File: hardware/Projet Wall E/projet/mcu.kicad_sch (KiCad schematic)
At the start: 11 parts, among them J3 Conn_01x06_Pin, U4 STM32G431RBTx

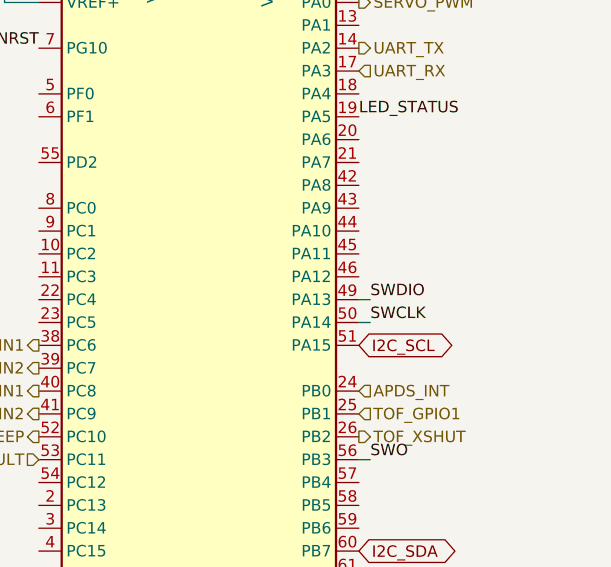
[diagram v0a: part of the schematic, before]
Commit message: Alim : BQ25896 + BQ27220, symboles perso wall_e, USB vers MCU
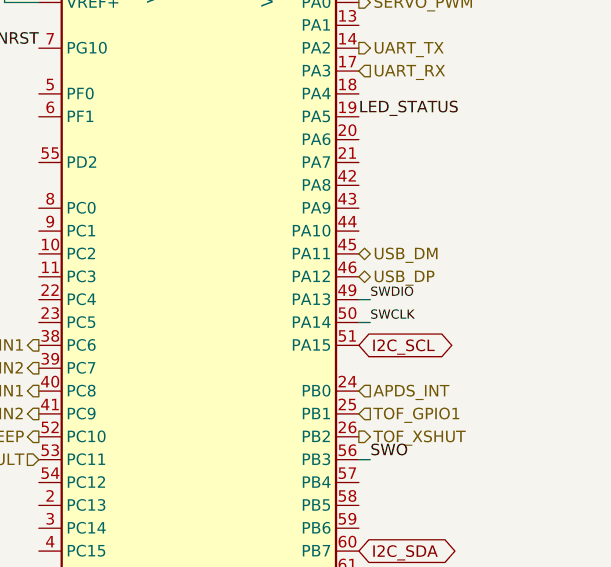
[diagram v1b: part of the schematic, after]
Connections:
- net USB_DM: now reaches U4.45 (PA11)
- net USB_DP: now reaches U4.46 (PA12)
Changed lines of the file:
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@@
 		(effects
 			(font
-				(size 1.27 1.27)
+				(size 1.016 1.016)
 			)
 			(justify left bottom)
@@
 		(effects
 			(font
-				(size 1.27 1.27)
+				(size 1.016 1.016)
 			)
 			(justify left bottom)
@@
 		)
 	)
+	(hierarchical_label "USB_DM"
+		(shape bidirectional)
+		(at 171.45 91.44 0)
+		(effects
+			(font
+				(size 1.27 1.27)
+			)
+			(justify left)
+		)
+	)
 	(hierarchical_label "MOT_AIN1"
 		(shape output)
@@
 		(effects
 			(font
+				(size 1.27 1.27)
+			)
+			(justify left)
+		)
+	)
+	(hierarchical_label "USB_DP"
+		(shape bidirectional)
+		(at 171.45 93.98 0)
+		(effects
+			(font

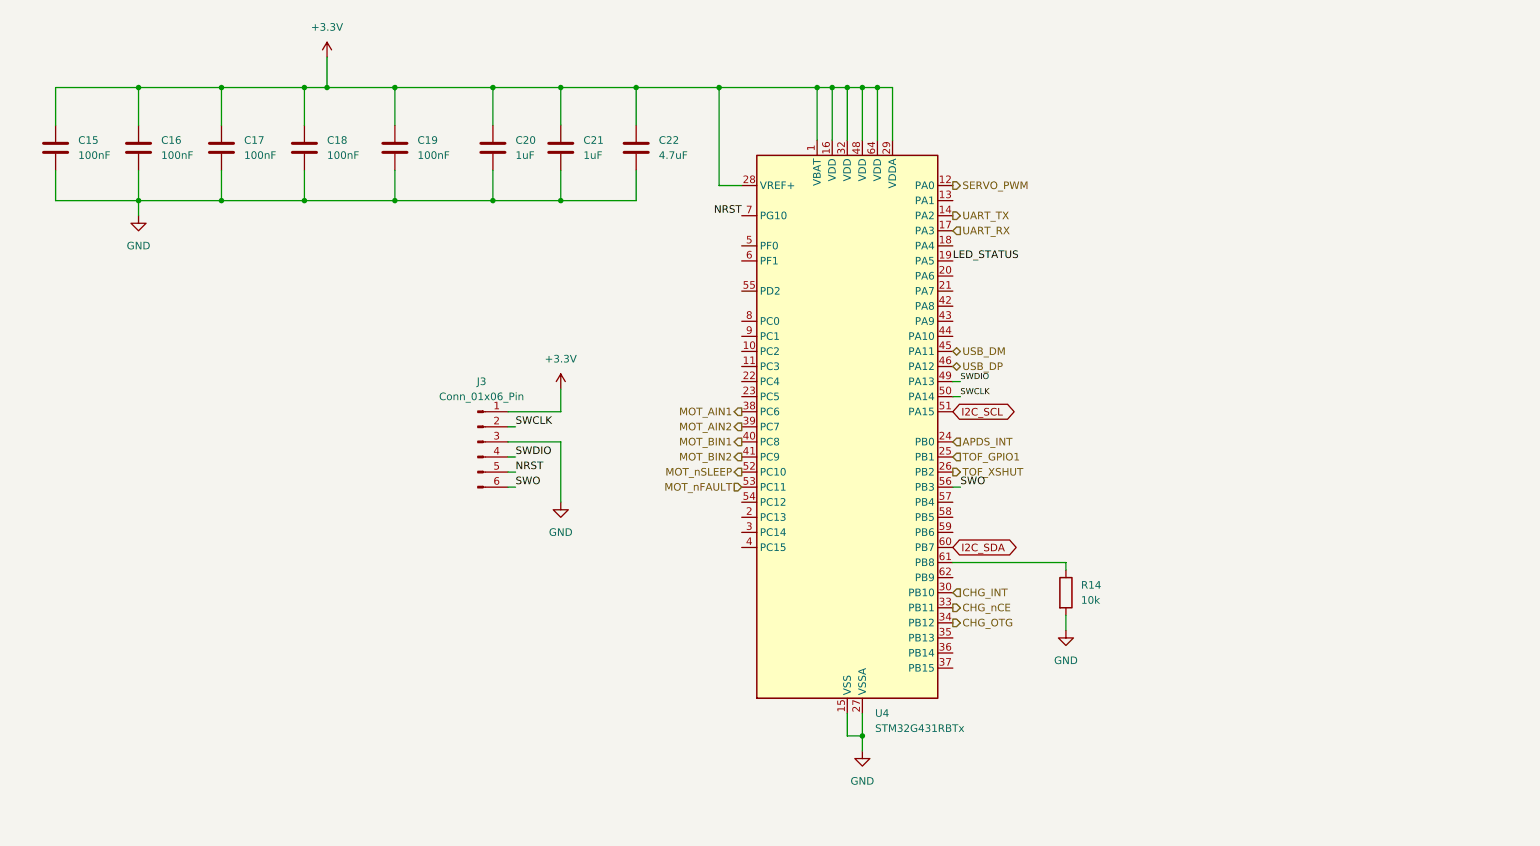
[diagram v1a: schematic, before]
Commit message: Mise à jour MCU + ajout du fichier .ioc
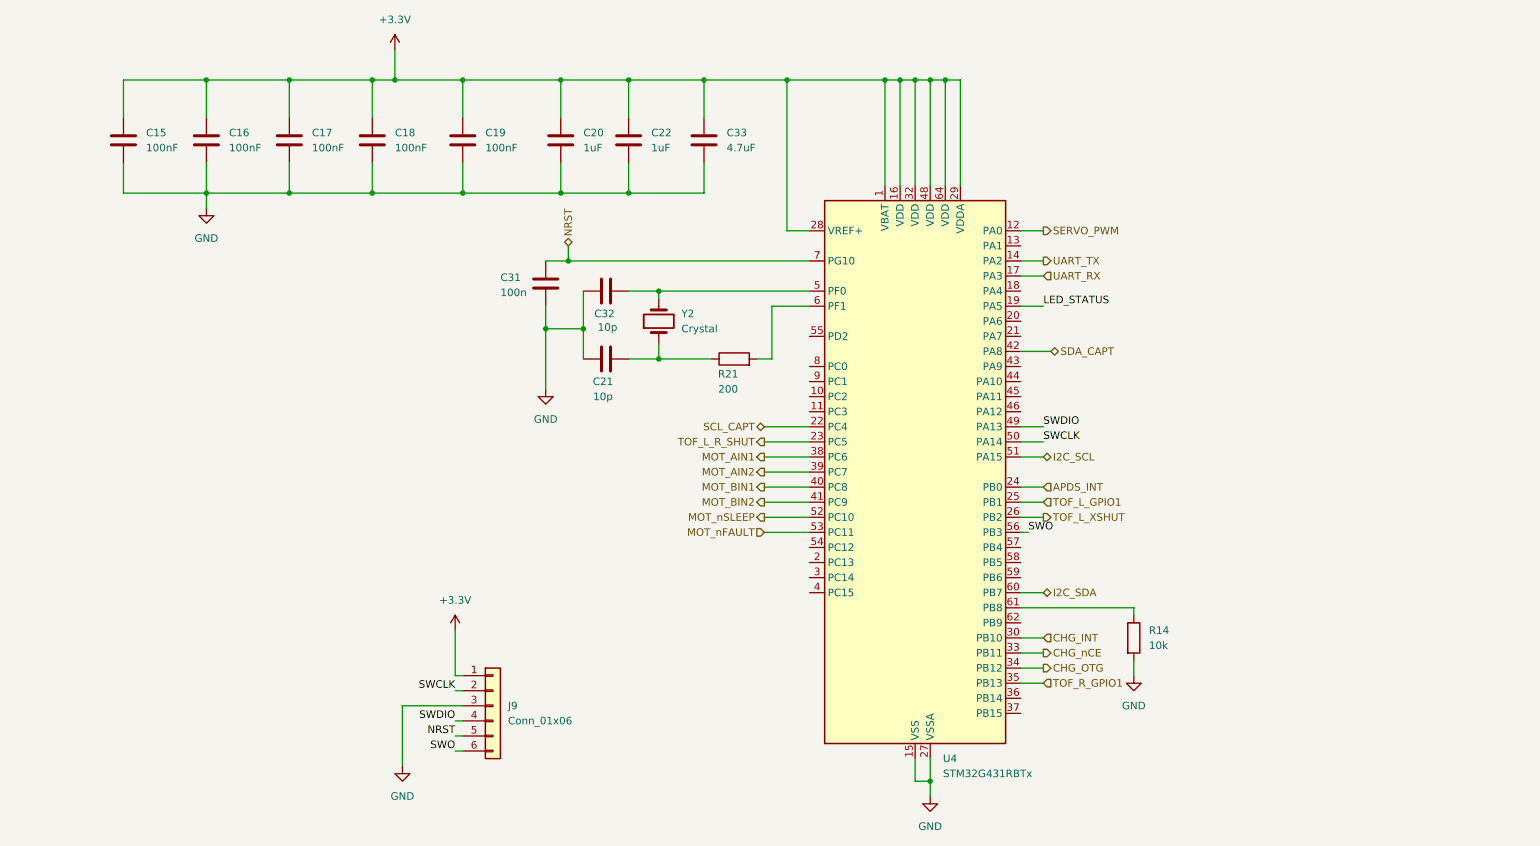
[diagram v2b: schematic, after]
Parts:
- removed J3: Conn_01x06_Pin, Connector_PinHeader_2.54mm:PinHeader_1x06_P2.54mm_Vertical, symbol wall_e:Conn_01x06_Pin
- added C31: 100n, Capacitor_SMD:C_0603_1608Metric, symbol wall_e:C
- added C32: 10p, Capacitor_SMD:C_0402_1005Metric, symbol wall_e:C
- added C33: 4.7uF, Capacitor_SMD:C_0603_1608Metric, symbol wall_e:C
- added J9: Conn_01x06, Connector_JST:JST_EH_S6B-EH_1x06_P2.50mm_Horizontal, symbol Connector_Generic:Conn_01x06
- added R21: 200, Resistor_SMD:R_0402_1005Metric, symbol wall_e:R
- added Y2: Crystal, symbol Device:Crystal
- C21: value 1uF -> 10p
- C22: value 4.7uF -> 1uF; footprint Capacitor_SMD:C_0603_1608Metric -> Capacitor_SMD:C_0402_1005Metric
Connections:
- net +3.3V: now also C33.1, J9.1 (Pin_1); no longer C21.1
- net GND: now also C21.1, C31.2, C32.1, C33.2, J9.3 (Pin_3); no longer C21.2
- net NRST: now also C31.1, J9.5 (Pin_5)
- net SWCLK: now also J9.2 (Pin_2)
- net SWDIO: now also J9.4 (Pin_4)
- net SWO: now also J9.6 (Pin_6)
- net SCL_CAPT: now reaches U4.22 (PC4)
- net TOF_L_R_SHUT: now reaches U4.23 (PC5)
- net TOF_R_GPIO1: now reaches U4.35 (PB13)
- net SDA_CAPT: now reaches U4.42 (PA8)
- net at U4.5 (PF0): now also C32.2, Y2.2
- net at U4.6 (PF1): now also R21.2
- net TOF_GPIO1 renamed TOF_L_GPIO1
- net TOF_XSHUT renamed TOF_L_XSHUT
- net USB_DM: no longer names the net of U4.45 (PA11)
- net USB_DP: no longer names the net of U4.46 (PA12)
- new net: C21.2, R21.1, Y2.1

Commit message: Add files via upload
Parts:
- removed J9: Conn_01x06, Connector_JST:JST_EH_S6B-EH_1x06_P2.50mm_Horizontal, symbol Connector_Generic:Conn_01x06
- removed R14: 10k, Resistor_SMD:R_01005_0402Metric, symbol wall_e:R
- removed R21: 200, Resistor_SMD:R_0402_1005Metric, symbol wall_e:R
- removed Y2: Crystal, symbol Device:Crystal
- added C23: 1uF, Capacitor_SMD:C_0402_1005Metric, symbol wall_e:C
- added D1: STATUS, LED_SMD:LED_0603_1608Metric, symbol Device:LED_Small
- added D2: POWER, LED_SMD:LED_0603_1608Metric, symbol Device:LED_Small
- added J1: Conn_01x03, Connector_Audio:Jack_XLR_Neutrik_NC3FAAH_Horizontal, symbol Connector_Generic:Conn_01x03
- added J2: Conn_ST_STDC14, Connector_PinHeader_1.27mm:PinHeader_2x07_P1.27mm_Vertical_SMD, symbol Connector:Conn_ST_STDC14
- added JP1, JP2: SolderJumper_2_Open, Jumper:SolderJumper-2_P1.3mm_Open_TrianglePad1.0x1.5mm, symbol Jumper:SolderJumper_2_Open
- added R3, R4: 1k, Resistor_SMD:R_0402_1005Metric, symbol Device:R_Small
- added Y1: 16MHz, Crystal:Crystal_SMD_EuroQuartz_MT-4Pin_3.2x2.5mm, symbol Device:Crystal_GND24_Small
- C19: value 100nF -> 4.7u
- C20: value 1uF -> 10n
- C33: value 4.7uF -> 100n
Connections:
- net +3.3V: now also C23.1, J1.1 (Pin_1), J2.3 (VCC), R3.1
- net GND: now also C23.2, D1.1 (K), D2.1 (K), J1.3 (Pin_3), J2.11 (GNDDetect), J2.5 (GND), J2.7 (GND), Y1.2 (G), Y1.4 (G)
- net LED_STATUS: now also R4.1
- net NRST: now also J2.12 (~{RST})
- net SERVO_PWM: now also U4.59 (PB6), J1.2 (Pin_2); no longer U4.12 (PA0)
- net SWCLK: now also J2.6 (JCLK/SWCLK)
- net SWDIO: now also J2.4 (JTMS/SWDIO)
- net SWO: now also J2.8 (JTDO/SWO)
- net ENCB_AOUT: now reaches U4.61 (PB8)
- net at C21.2: now also U4.6 (PF1), Y1.3
- net at C32.2, U4.5 (PF0): now also Y1.1
- net ENCB_BOUT: now reaches U4.43 (PA9)
- net ENCA_BOUT: now reaches U4.44 (PA10)
- net ENCA_AOUT: now reaches U4.62 (PB9)
- net TOF_L_R_SHUT renamed TOF_R_SHUT
- net UART_RX renamed VCP_RX
- net VCP_RX: now also JP1.1 (A)
- net UART_TX renamed VCP_TX
- net VCP_TX: now also JP2.1 (A)
- new net: J2.13 (VCP_RX), JP1.2 (B)
- new net: D1.2 (A), R4.2
- new net: J2.14 (VCP_TX), JP2.2 (B)
- new net: D2.2 (A), R3.2
- no-connect marks 0 -> 2
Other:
- moved on the sheet: C15, C16, C17, C18, C19, C20, C21, C22, C32, C33

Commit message: feat: mise a jour alim reference jlcpcb
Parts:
- C15, C16, C17, C18: JLCPCB Part # (none) -> C1525
- C20: JLCPCB Part # (none) -> C15195
- U4: JLCPCB Part # (none) -> C431633
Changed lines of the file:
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@@
 		)
 		(instances
+			(project "projet"
+				(path "/aad9219d-d686-4d68-8dbb-b3c2b0727159/8d7235a3-ed0d-4c0c-a716-b22c65fe70a8"
+					(reference "J1")
+					(unit 1)
+				)
+			)
 			(project "mcu"
 				(path "/d1f6b90d-1ee5-4a93-8c97-f2b0d96541e8"
@@
 		)
 		(instances
+			(project "projet"
+				(path "/aad9219d-d686-4d68-8dbb-b3c2b0727159/8d7235a3-ed0d-4c0c-a716-b22c65fe70a8"
+					(reference "#PWR016")
+					(unit 1)
+				)
+			)
 			(project "mcu"
 				(path "/d1f6b90d-1ee5-4a93-8c97-f2b0d96541e8"
@@
 			)
 		)
+		(property "JLCPCB Part #" "C15195"
+			(at 88.9 55.88 0)
+			(hide yes)
+			(show_name no)
+			(do_not_autoplace no)
+			(effects
+				(font
+					(size 1.27 1.27)
+				)
+			)
+		)
 		(pin "2"
 		)
@@
 		)
 		(instances
+			(project "projet"
+				(path "/aad9219d-d686-4d68-8dbb-b3c2b0727159/8d7235a3-ed0d-4c0c-a716-b22c65fe70a8"
+					(reference "JP1")
+					(unit 1)
+				)
+			)
 			(project "mcu"
 				(path "/d1f6b90d-1ee5-4a93-8c97-f2b0d96541e8"
@@
 		)
 		(instances
+			(project "projet"
+				(path "/aad9219d-d686-4d68-8dbb-b3c2b0727159/8d7235a3-ed0d-4c0c-a716-b22c65fe70a8"
+					(reference "#PWR034")
+					(unit 1)
+				)
+			)
 			(project "mcu"
 				(path "/d1f6b90d-1ee5-4a93-8c97-f2b0d96541e8"
@@
 		)
 		(instances
+			(project "projet"
+				(path "/aad9219d-d686-4d68-8dbb-b3c2b0727159/8d7235a3-ed0d-4c0c-a716-b22c65fe70a8"
+					(reference "#PWR017")
+					(unit 1)
+				)
+			)
 			(project "mcu"
 				(path "/d1f6b90d-1ee5-4a93-8c97-f2b0d96541e8"
@@
 		)
 		(instances
+			(project "projet"
+				(path "/aad9219d-d686-4d68-8dbb-b3c2b0727159/8d7235a3-ed0d-4c0c-a716-b22c65fe70a8"
+					(reference "D1")
+					(unit 1)
+				)
+			)
 			(project "mcu"
 				(path "/d1f6b90d-1ee5-4a93-8c97-f2b0d96541e8"
@@
 		)
 		(instances
+			(project "projet"
+				(path "/aad9219d-d686-4d68-8dbb-b3c2b0727159/8d7235a3-ed0d-4c0c-a716-b22c65fe70a8"
+					(reference "JP2")
+					(unit 1)
+				)
+			)
 			(project "mcu"
 				(path "/d1f6b90d-1ee5-4a93-8c97-f2b0d96541e8"
@@
 		)
 		(instances
+			(project "projet"
+				(path "/aad9219d-d686-4d68-8dbb-b3c2b0727159/8d7235a3-ed0d-4c0c-a716-b22c65fe70a8"
+					(reference "#PWR035")
+					(unit 1)
+				)
+			)
 			(project "mcu"
 				(path "/d1f6b90d-1ee5-4a93-8c97-f2b0d96541e8"
@@
 			)
 		)
+		(property "JLCPCB Part #" "C1525"
+			(at 29.21 55.88 0)
+			(hide yes)
+			(show_name no)
+			(do_not_autoplace no)
+			(effects
+				(font
+					(size 1.27 1.27)
+				)
+			)
+		)
 		(pin "2"
 		)
@@
 			)
 		)
+		(property "JLCPCB Part #" "C431633"
+			(at 165.1 111.76 0)
+			(hide yes)
+			(show_name no)
+			(do_not_autoplace no)
+			(effects
+				(font
+					(size 1.27 1.27)
+				)
+			)
+		)
 		(pin "9"
 		)
@@
 			)
 		)
+		(property "JLCPCB Part #" "C1525"
+			(at 57.15 55.88 0)
+			(hide yes)
+			(show_name no)
+			(do_not_autoplace no)
+			(effects
+				(font
+					(size 1.27 1.27)
+				)
+			)
+		)
 		(pin "2"
 		)
@@
 		)
 		(instances
+			(project "projet"
+				(path "/aad9219d-d686-4d68-8dbb-b3c2b0727159/8d7235a3-ed0d-4c0c-a716-b22c65fe70a8"
+					(reference "#PWR013")
+					(unit 1)
+				)
+			)
 			(project "mcu"
 				(path "/d1f6b90d-1ee5-4a93-8c97-f2b0d96541e8"
@@
 		)
 		(instances
+			(project "projet"
+				(path "/aad9219d-d686-4d68-8dbb-b3c2b0727159/8d7235a3-ed0d-4c0c-a716-b22c65fe70a8"
+					(reference "#PWR015")
+					(unit 1)
+				)
+			)
 			(project "mcu"
 				(path "/d1f6b90d-1ee5-4a93-8c97-f2b0d96541e8"
@@
 		)
 		(instances
+			(project "projet"
+				(path "/aad9219d-d686-4d68-8dbb-b3c2b0727159/8d7235a3-ed0d-4c0c-a716-b22c65fe70a8"
+					(reference "Y1")
+					(unit 1)
+				)
+			)
 			(project "mcu"
 				(path "/d1f6b90d-1ee5-4a93-8c97-f2b0d96541e8"
@@
 			)
 		)
+		(property "JLCPCB Part #" "C1525"
+			(at 43.18 55.88 0)
+			(hide yes)
+			(show_name no)
+			(do_not_autoplace no)
+			(effects
+				(font
+					(size 1.27 1.27)
+				)
+			)
+		)
 		(pin "2"
 		)
@@
 		)
 		(instances
+			(project "projet"
+				(path "/aad9219d-d686-4d68-8dbb-b3c2b0727159/8d7235a3-ed0d-4c0c-a716-b22c65fe70a8"
+					(reference "J2")
+					(unit 1)
+				)
+			)
 			(project "mcu"
 				(path "/d1f6b90d-1ee5-4a93-8c97-f2b0d96541e8"
@@
 		)
 		(instances
+			(project "projet"
+				(path "/aad9219d-d686-4d68-8dbb-b3c2b0727159/8d7235a3-ed0d-4c0c-a716-b22c65fe70a8"
+					(reference "R4")
+					(unit 1)
+				)
+			)
 			(project "mcu"
 				(path "/d1f6b90d-1ee5-4a93-8c97-f2b0d96541e8"
@@
 			)
 		)
+		(property "JLCPCB Part #" "C1525"
+			(at 15.24 55.88 0)
+			(hide yes)
+			(show_name no)
+			(do_not_autoplace no)
+			(effects
+				(font
+					(size 1.27 1.27)
+				)
+			)
+		)
 		(pin "2"
 		)
@@
 		)
 		(instances
+			(project "projet"
+				(path "/aad9219d-d686-4d68-8dbb-b3c2b0727159/8d7235a3-ed0d-4c0c-a716-b22c65fe70a8"
+					(reference "R3")
+					(unit 1)
+				)
+			)
 			(project "mcu"
 				(path "/d1f6b90d-1ee5-4a93-8c97-f2b0d96541e8"
@@
 		)
 		(instances
+			(project "projet"
+				(path "/aad9219d-d686-4d68-8dbb-b3c2b0727159/8d7235a3-ed0d-4c0c-a716-b22c65fe70a8"
+					(reference "D2")
+					(unit 1)
+				)
+			)
 			(project "mcu"
 				(path "/d1f6b90d-1ee5-4a93-8c97-f2b0d96541e8"
@@
 		)
 		(instances
+			(project "projet"
+				(path "/aad9219d-d686-4d68-8dbb-b3c2b0727159/8d7235a3-ed0d-4c0c-a716-b22c65fe70a8"
+					(reference "C23")
+					(unit 1)
+				)
+			)
 			(project "mcu"
 				(path "/d1f6b90d-1ee5-4a93-8c97-f2b0d96541e8"
@@
 		)
 	)
-	(embedded_fonts no)
 )
